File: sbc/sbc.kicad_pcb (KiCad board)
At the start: 2 copper layers, 19 parts, among them J1 USB_B_Micro, J2 PB, J3 PA, SW1 RESET, U1 DS1813, U2 WD65C02, U3 28C256, U4 HM62256BLP, U5 WD65C22, U6 7400, X1 CXO_DIP14

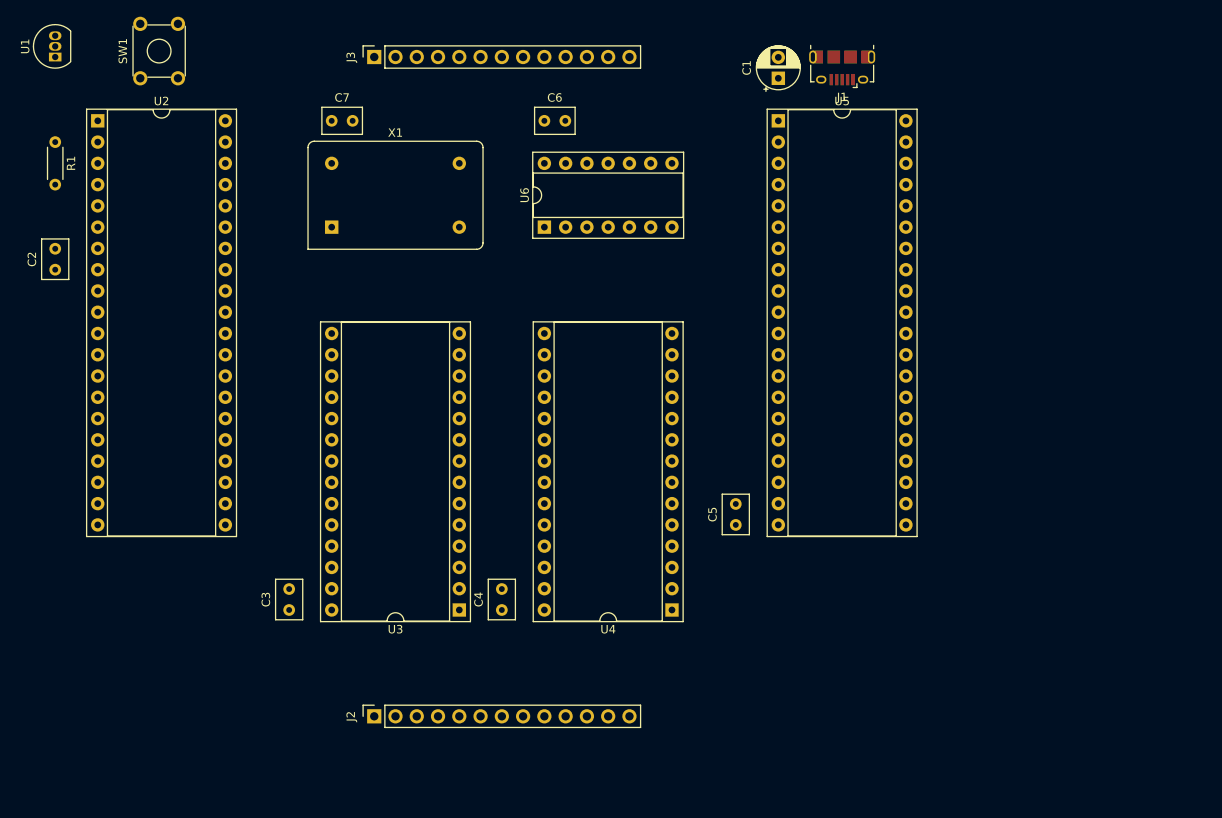
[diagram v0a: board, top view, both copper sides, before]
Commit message: SBC: Wire up memories
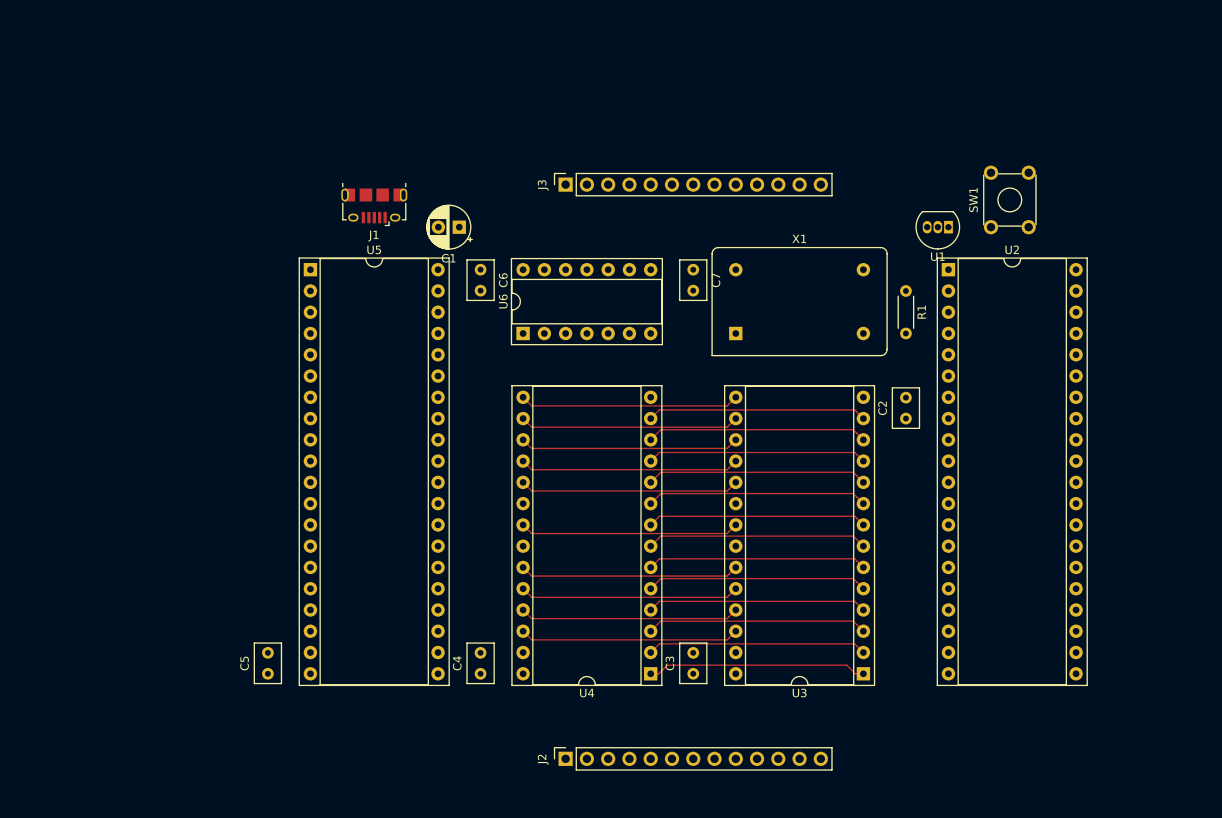
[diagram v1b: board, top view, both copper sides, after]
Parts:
- moved U1 108.6 mm to (177.8, 63.5), turned to 180 degrees
- moved U2 103.1 mm to (177.8, 68.6)
- moved C2 103.1 mm to (172.7, 86.4)
- moved R1 103.1 mm to (172.7, 71.1)
- moved SW1 103.1 mm to (182.9, 63.5)
- moved C5 58.6 mm to (96.5, 116.8)
- moved U5 58.6 mm to (101.6, 68.6)
- moved J1 58.3 mm to (109.2, 61.0)
- moved X1 49.9 mm to (152.4, 76.2)
- moved C3 48.9 mm to (147.3, 116.8)
- moved U3 48.9 mm to (167.6, 116.8)
- moved C7 46.7 mm to (147.3, 68.6), turned to 270 degrees
- moved C1 42.0 mm to (119.4, 63.5), turned to 180 degrees
- moved J3 27.5 mm to (132.1, 58.4)
- moved J2 23.4 mm to (132.1, 127.0)
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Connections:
- U6 pad 1: /A15 -> Net-(U2-Pad37)
- U6 pad 2: /A15 -> Net-(U3-Pad20)
- U6 pad 3: Net-(U3-Pad20) -> Net-(U4-Pad20)
- U6 pad 4: Net-(U2-Pad37) -> /A15
- U6 pad 5: Net-(U3-Pad20) -> /A15
- U6 pad 6: Net-(U4-Pad20) -> Net-(U3-Pad20)
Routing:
- net /D1: track 0.00 -> 26.4 mm
- net /A7: track 0.00 -> 26.4 mm
- net /A5: track 0.00 -> 26.4 mm
- net /A0: track 0.00 -> 26.4 mm
- net /A3: track 0.00 -> 26.4 mm
- net /A1: track 0.00 -> 26.4 mm
- net /D6: track 0.00 -> 26.3 mm
- net /D3: track 0.00 -> 26.3 mm
- net /A2: track 0.00 -> 26.3 mm
- net /D7: track 0.00 -> 26.3 mm
- net /D5: track 0.00 -> 26.3 mm
- net /D4: track 0.00 -> 26.3 mm
- net /A9: track 0.00 -> 26.3 mm
- net /A8: track 0.00 -> 26.3 mm
- net /A13: track 0.00 -> 26.3 mm
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
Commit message: SBC: Wire up signals
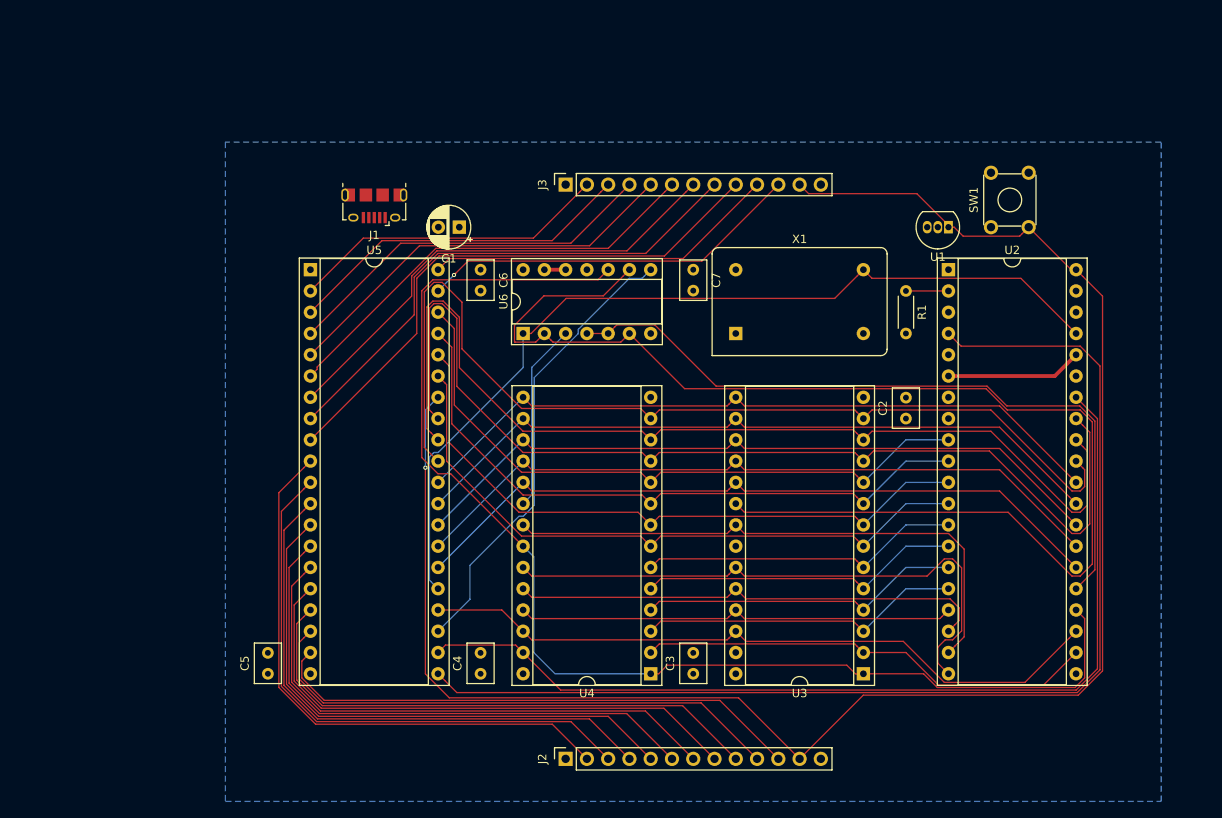
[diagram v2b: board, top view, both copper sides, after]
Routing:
- net Net-(J2-Pad12): track 0.00 -> 210.6 mm, vias 0 -> 1
- net Net-(U3-Pad20): track 0.00 -> 156.8 mm
- net Net-(U2-Pad4): track 0.00 -> 137.1 mm
- net /A14: track 26.3 -> 150.3 mm
- net Net-(U2-Pad34): track 0.00 -> 115.9 mm
- net Net-(U2-Pad37): track 0.00 -> 108.2 mm
- net /D0: track 26.3 -> 124.4 mm
- net /D1: track 26.4 -> 120.1 mm
- net /D2: track 26.3 -> 119.2 mm
- net /A15: track 0.00 -> 86.8 mm
- net /PB0: track 0.00 -> 68.9 mm
- net /PB1: track 0.00 -> 68.4 mm
- net /PB2: track 0.00 -> 67.9 mm
- net /PB3: track 0.00 -> 67.4 mm
- net /PA7: track 0.00 -> 67.3 mm
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- added copper zone on B.Cu, net GND

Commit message: SBC: Wire up power and ground
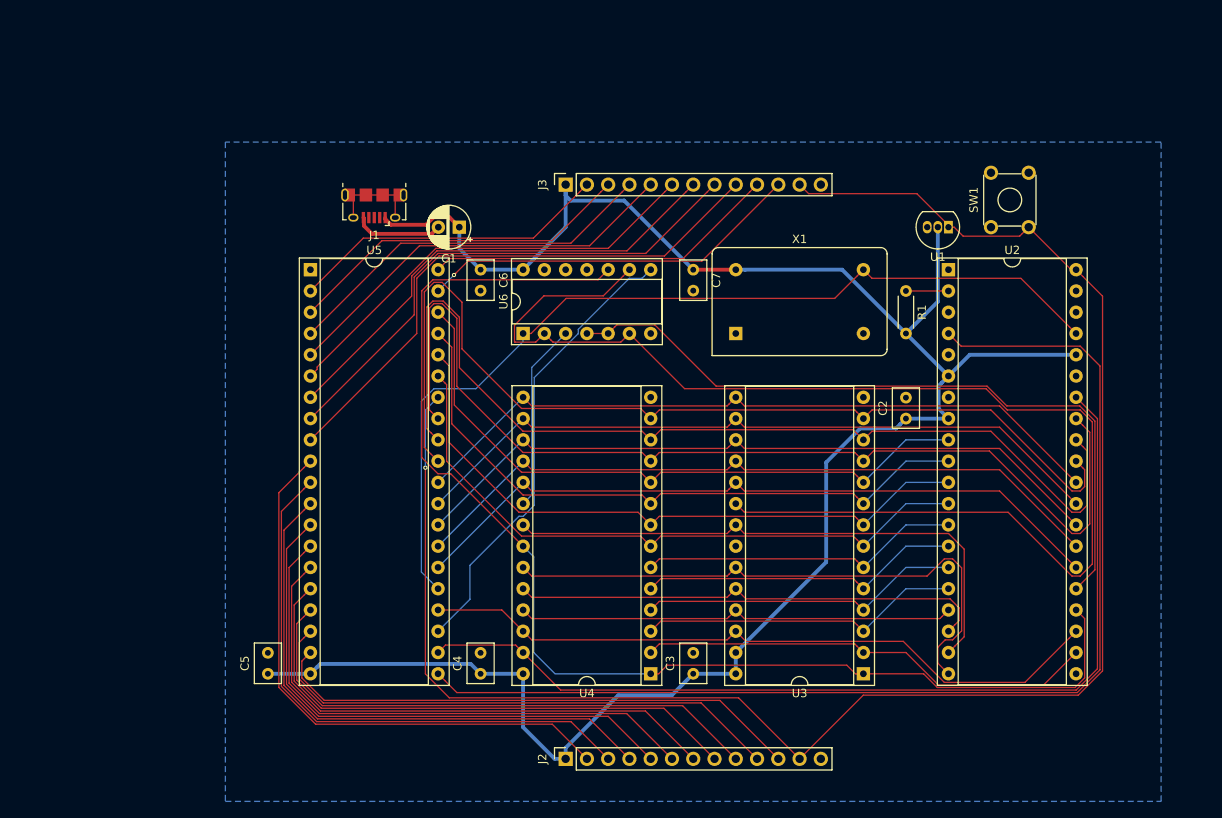
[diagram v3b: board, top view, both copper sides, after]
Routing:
- net +5V: track 16.3 -> 242.5 mm
- net Net-(J1-Pad6): track 0.00 -> 11.5 mm
- net Net-(C1-Pad2): track 0.00 -> 10.6 mm
- net Net-(U2-Pad37): track 108.2 -> 111.6 mm
- net GND: track 2.54 -> 0.00 mm

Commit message: SBC: Add mounting holes and polish silkscreen
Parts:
- added M1: M2.5, mounting_hole:MountingHole_2.7mm_M2.5_Pad, F.Cu at (96.5, 58.4)
- added M2: M2.5, mounting_hole:MountingHole_2.7mm_M2.5_Pad, F.Cu at (198.1, 58.4)
- added M3: M2.5, mounting_hole:MountingHole_2.7mm_M2.5_Pad, F.Cu at (96.5, 127.0)
- added M4: M2.5, mounting_hole:MountingHole_2.7mm_M2.5_Pad, F.Cu at (198.1, 127.0)
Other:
- board text added: "v1.0 © 2021 Daniel Picken https://github.com/dpicken/6502-hw"
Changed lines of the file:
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@@
 (kicad_pcb (version 20171130) (host pcbnew 5.1.4+dfsg1-1~bpo10+1)
   (general
-    (thickness 0.8128)
-    (drawings 0)
+    (thickness 1.6002)
+    (drawings 1)
     (tracks 546)
     (zones 0)
-    (modules 19)
+    (modules 23)
     (nets 71)
   )
@@
   (title_block
     (title "6502 SBC")
+    (date 2021-09-09)
     (rev 1.0)
   )
@@
     (add_net "Net-(C1-Pad2)")
   )
+  (module mounting_hole:MountingHole_2.7mm_M2.5_Pad (layer F.Cu)
+    (at 198.12 58.42)
+    (descr "Mounting Hole 2.7mm, M2.5")
+    (tags "mounting hole 2.7mm m2.5")
+    (attr virtual)
+    (fp_text reference M2 (at 0 -3.7) (layer F.SilkS)
+      (effects (font (size 1 1) (thickness 0.15)))
+    )
+    (fp_text value M2.5 (at 0 3.7) (layer F.Fab)
+      (effects (font (size 1 1) (thickness 0.15)))
+    )
+    (fp_circle (center 0 0) (end 2.95 0) (layer F.CrtYd) (width 0.05))
+    (fp_circle (center 0 0) (end 2.7 0) (layer Cmts.User) (width 0.15))
+    (fp_text user %R (at 0.3 0) (layer F.Fab)
+      (effects (font (size 1 1) (thickness 0.15)))
+    )
+    (pad 1 thru_hole circle (at 0 0) (size 5.4 5.4) (drill 2.7) (layers *.Cu *.Mask))
+  )
+  (module mounting_hole:MountingHole_2.7mm_M2.5_Pad (layer F.Cu)
+    (at 96.52 58.42)
+    (descr "Mounting Hole 2.7mm, M2.5")
+    (tags "mounting hole 2.7mm m2.5")
+    (attr virtual)
+    (fp_text reference M1 (at 0 -3.7) (layer F.SilkS)
+      (effects (font (size 1 1) (thickness 0.15)))
+    )
+    (fp_text value M2.5 (at 0 3.7) (layer F.Fab)
+      (effects (font (size 1 1) (thickness 0.15)))
+    )
+    (fp_circle (center 0 0) (end 2.95 0) (layer F.CrtYd) (width 0.05))
+    (fp_circle (center 0 0) (end 2.7 0) (layer Cmts.User) (width 0.15))
+    (fp_text user %R (at 0.3 0) (layer F.Fab)
+      (effects (font (size 1 1) (thickness 0.15)))
+    )
+    (pad 1 thru_hole circle (at 0 0) (size 5.4 5.4) (drill 2.7) (layers *.Cu *.Mask))
+  )
+  (module mounting_hole:MountingHole_2.7mm_M2.5_Pad (layer F.Cu)
+    (at 96.52 127)
+    (descr "Mounting Hole 2.7mm, M2.5")
+    (tags "mounting hole 2.7mm m2.5")
+    (attr virtual)
+    (fp_text reference M3 (at 0 -3.7) (layer F.SilkS)
+      (effects (font (size 1 1) (thickness 0.15)))
+    )
+    (fp_text value M2.5 (at 0 3.7) (layer F.Fab)
+      (effects (font (size 1 1) (thickness 0.15)))
+    )
+    (fp_circle (center 0 0) (end 2.95 0) (layer F.CrtYd) (width 0.05))
+    (fp_circle (center 0 0) (end 2.7 0) (layer Cmts.User) (width 0.15))
+    (fp_text user %R (at 0.3 0) (layer F.Fab)
+      (effects (font (size 1 1) (thickness 0.15)))
+    )
+    (pad 1 thru_hole circle (at 0 0) (size 5.4 5.4) (drill 2.7) (layers *.Cu *.Mask))
+  )
+  (module mounting_hole:MountingHole_2.7mm_M2.5_Pad (layer F.Cu)
+    (at 198.12 127)
+    (descr "Mounting Hole 2.7mm, M2.5")
+    (tags "mounting hole 2.7mm m2.5")
+    (attr virtual)
+    (fp_text reference M4 (at 0 -3.7) (layer F.SilkS)
+      (effects (font (size 1 1) (thickness 0.15)))
+    )
+    (fp_text value M2.5 (at 0 3.7) (layer F.Fab)
+      (effects (font (size 1 1) (thickness 0.15)))
+    )
+    (fp_circle (center 0 0) (end 2.95 0) (layer F.CrtYd) (width 0.05))
+    (fp_circle (center 0 0) (end 2.7 0) (layer Cmts.User) (width 0.15))
+    (fp_text user %R (at 0.3 0) (layer F.Fab)
+      (effects (font (size 1 1) (thickness 0.15)))
+    )
+    (pad 1 thru_hole circle (at 0 0) (size 5.4 5.4) (drill 2.7) (layers *.Cu *.Mask))
+  )
   (module dip:DIP-28_W15.24mm_Socket (layer F.Cu)
     (at 167.64 116.84 180)
@@
     (descr "CP, Radial series, Radial, pin pitch=2.50mm, , diameter=5mm, Electrolytic Capacitor")
     (tags "CP Radial series Radial pin pitch 2.50mm  diameter 5mm Electrolytic Capacitor")
-    (fp_text reference C1 (at 1.25 -3.75) (layer F.SilkS)
+    (fp_text reference C1 (at 1.25 3.81) (layer F.SilkS)
       (effects (font (size 1 1) (thickness 0.15)))
     )
@@
     (descr "C, Rect series, Radial, pin pitch=2.50mm, , length*width=4.6*3.0mm^2, Capacitor, http://www.wima.de/DE/WIMA_MKS_02.pdf")
     (tags "C Rect series Radial pin pitch 2.50mm  length 4.6mm width 3.0mm Capacitor")
-    (fp_text reference C6 (at 1.25 -2.75 90) (layer F.SilkS)
+    (fp_text reference C6 (at 1.27 2.54 90) (layer F.SilkS)
       (effects (font (size 1 1) (thickness 0.15)))
     )
@@
     (descr "C, Rect series, Radial, pin pitch=2.50mm, , length*width=4.6*3.0mm^2, Capacitor, http://www.wima.de/DE/WIMA_MKS_02.pdf")
     (tags "C Rect series Radial pin pitch 2.50mm  length 4.6mm width 3.0mm Capacitor")
-    (fp_text reference C7 (at 1.25 -2.75 90) (layer F.SilkS)
+    (fp_text reference C7 (at 1.27 2.54 90) (layer F.SilkS)
       (effects (font (size 1 1) (thickness 0.15)))
     )
@@
     (tags "USB Micro B horizontal SMD")
     (attr smd)
-    (fp_text reference J1 (at 0 -3.5) (layer F.SilkS)
+    (fp_text reference J1 (at 0 3.81) (layer F.SilkS)
       (effects (font (size 1 1) (thickness 0.15)))
     )
@@
     (descr "TO-92 leads in-line, narrow, oval pads, drill 0.75mm (see NXP sot054_po.pdf)")
     (tags "to-92 sc-43 sc-43a sot54 PA33 transistor")
-    (fp_text reference U1 (at 1.27 -3.56) (layer F.SilkS)
+    (fp_text reference U1 (at 1.27 2.54) (layer F.SilkS)
       (effects (font (size 1 1) (thickness 0.15)))
     )
@@
     )
   )
+  (gr_text "v1.0\n© 2021 Daniel Picken\nhttps://github.com/dpicken/6502-hw" (at 101.6 127) (layer F.SilkS)
+    (effects (font (size 0.762 0.762) (thickness 0.127)) (justify left))
+  )
   (segment (start 121.92 116.84) (end 127 116.84) (width 0.4572) (layer B.Cu) (net 1))

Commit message: SBC: Add board outline
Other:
- board outline added: 111.8 x 78.7 mm
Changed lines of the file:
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@@
   (general
     (thickness 1.6002)
-    (drawings 1)
+    (drawings 5)
     (tracks 546)
     (zones 0)
@@
     )
   )
+  (gr_line (start 91.44 53.34) (end 91.44 132.08) (layer Edge.Cuts) (width 0.05))
+  (gr_line (start 203.2 53.34) (end 91.44 53.34) (layer Edge.Cuts) (width 0.05))
+  (gr_line (start 203.2 132.08) (end 203.2 53.34) (layer Edge.Cuts) (width 0.05))
+  (gr_line (start 91.44 132.08) (end 203.2 132.08) (layer Edge.Cuts) (width 0.05))
   (gr_text "v1.0\n© 2021 Daniel Picken\nhttps://github.com/dpicken/6502-hw" (at 101.6 127) (layer F.SilkS)
     (effects (font (size 0.762 0.762) (thickness 0.127)) (justify left))
